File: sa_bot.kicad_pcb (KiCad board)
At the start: 2 copper layers, 120 x 120 mm, 66 parts, among them CON1 MicroSD_Card, P1 USB_OTG, P11 MOTOR_A, P12 MOTOR_B, P13 SONAR_4, P14 SONAR_2, P15 SONAR_3, P17 DBG_CONN, P18 CONN_01X04, P2 BatteryHolder, P3 IR4_JMP, P4 IR2_JMP, P5 IR3_JMP, P6 ExPower, P7 IR_4, P8 IR_2, P9 IR_3, Q1 Q_PMOS_DSG, SW1 SWITCH_INV, SW2 SW_PUSH, SW3 SW_PUSH, U1 74AHC1G125, U2 SAMD21G18, U3 AP2112K-3.3V, U4 NCP1402, U5 DRV8835, Y1 Crystal_Small

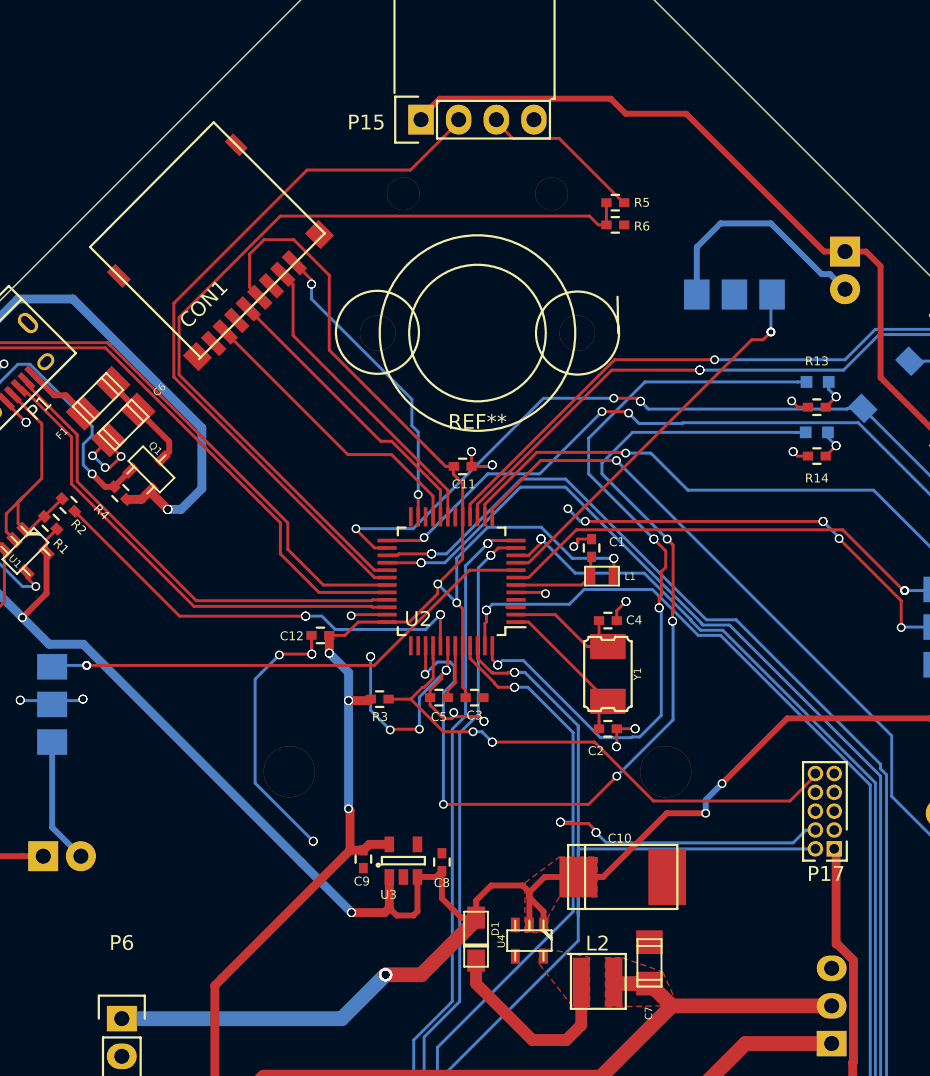
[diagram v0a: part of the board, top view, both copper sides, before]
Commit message: Moved RXTX LEDs
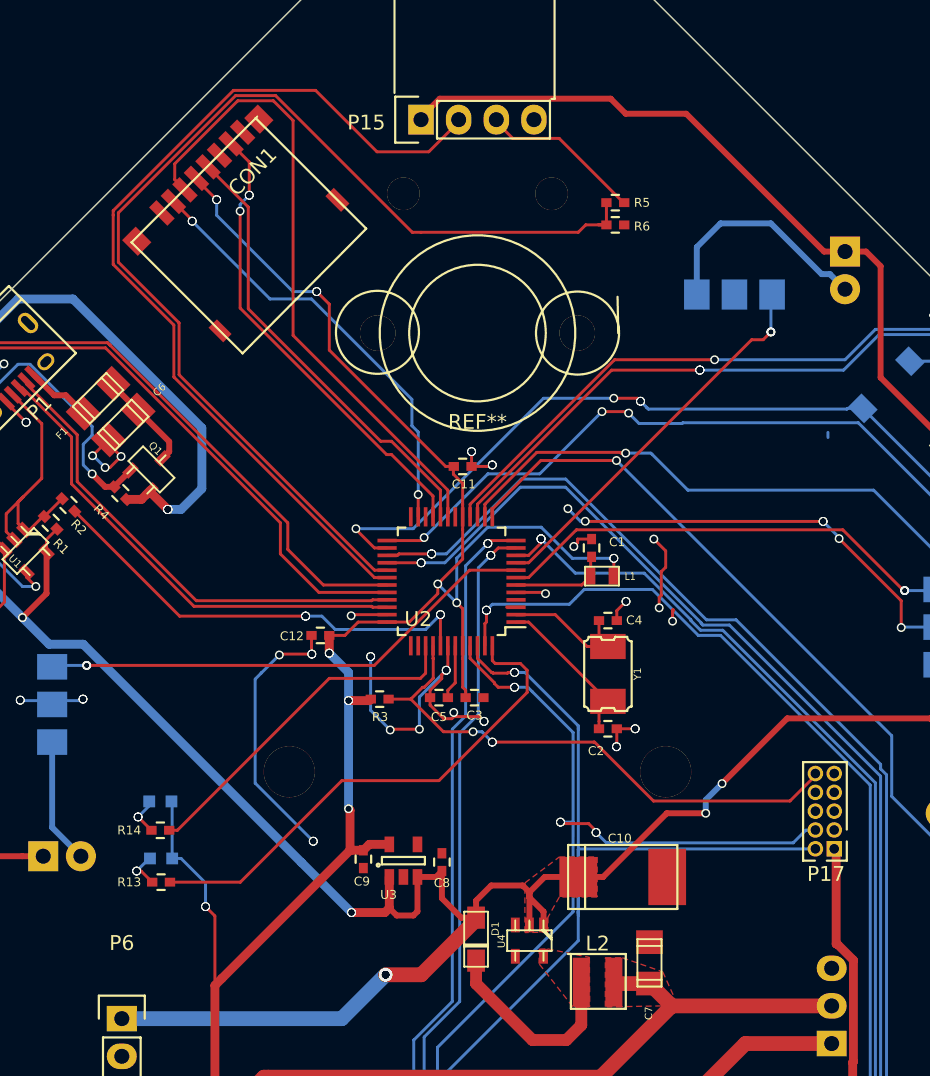
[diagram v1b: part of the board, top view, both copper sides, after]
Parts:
- moved D6 54.7 mm to (118.7, 159.8), turned to 180 degrees
- moved R13 54.6 mm to (118.7, 161.4), turned to 180 degrees
- moved R14 51.0 mm to (118.6, 157.9), turned to 180 degrees
- moved D7 50.8 mm to (118.6, 156.0), turned to 180 degrees
- moved CON1 14.4 mm to (124.2, 110.8), turned to 225 degrees
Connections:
- net /IR1 renamed Net-(U2-Pad3)
- net VCC renamed +5V
- CON1 pad 1: /SD_CS -> Net-(CON1-Pad1)
- CON1 pad 2: /SPI_MOSI -> /SD_CS
- CON1 pad 3: GND -> /SPI_MOSI
- D6 pad 2: /RXLED -> +3V3
- D7 pad 2: /TXLED -> +3V3
- R13 pad 1: GND -> /RXLED
- R14 pad 1: GND -> /TXLED
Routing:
- net /TXLED: track 66.0 -> 23.5 mm, vias 6 -> 0
- net /SPI_MOSI: track 21.0 -> 43.4 mm
- net /RXLED: track 52.8 -> 34.5 mm, vias 6 -> 0
- net /ECHO3: track 56.8 -> 74.4 mm
- net +3V3: track 209.0 -> 224.2 mm, vias 12 -> 18
- net /TRIG3: track 49.4 -> 62.3 mm
- net /SPI_MISO: track 20.0 -> 31.5 mm, vias 0 -> 3
- net /SPI_SCK: track 19.8 -> 30.5 mm
- net /SD_CS: track 20.6 -> 29.8 mm
- net (no net): track 1.16 -> 7.58 mm, vias 2 -> 5
- net GND: track 161.2 -> 158.8 mm, vias 76 -> 73
- net Net-(D7-Pad1): track 2.12 -> 2.63 mm
- added copper zone on F.Cu, net VCC
- removed copper zone on F.Cu, net +5V

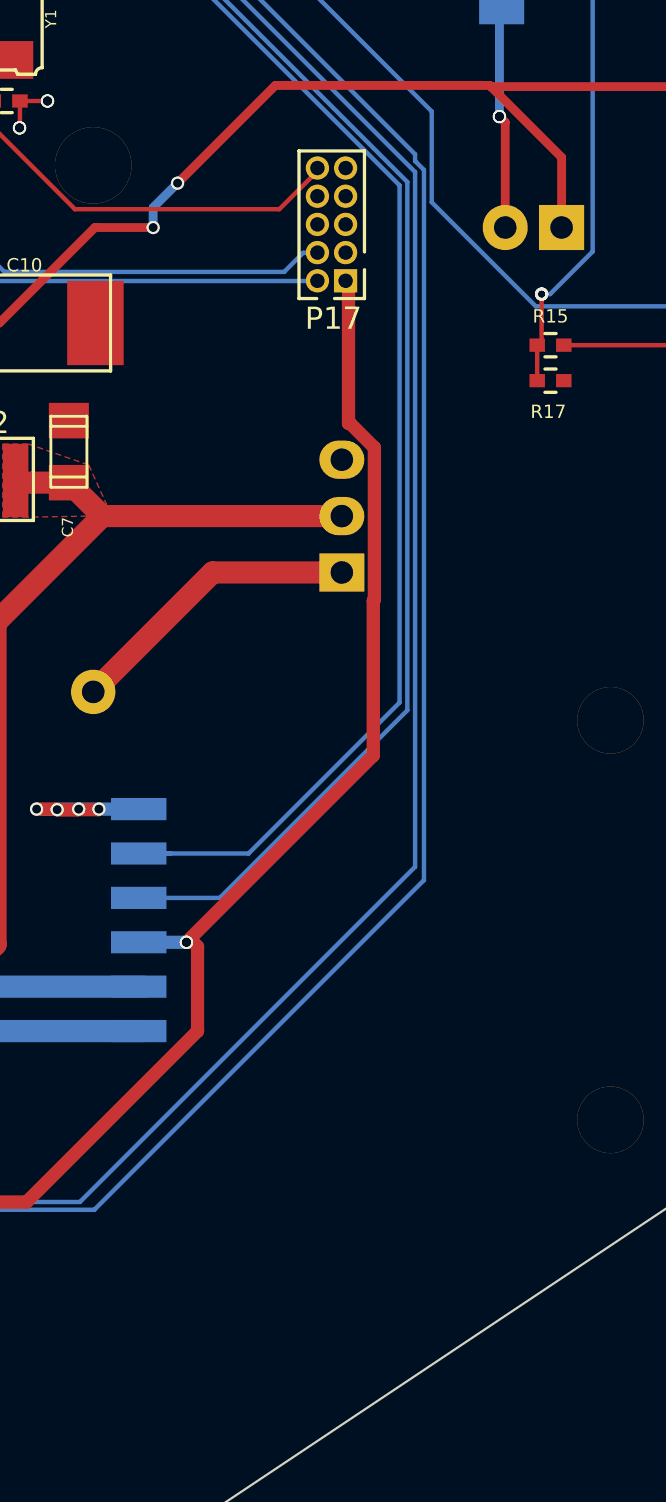
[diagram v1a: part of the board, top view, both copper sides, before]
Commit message: Added Reset Button
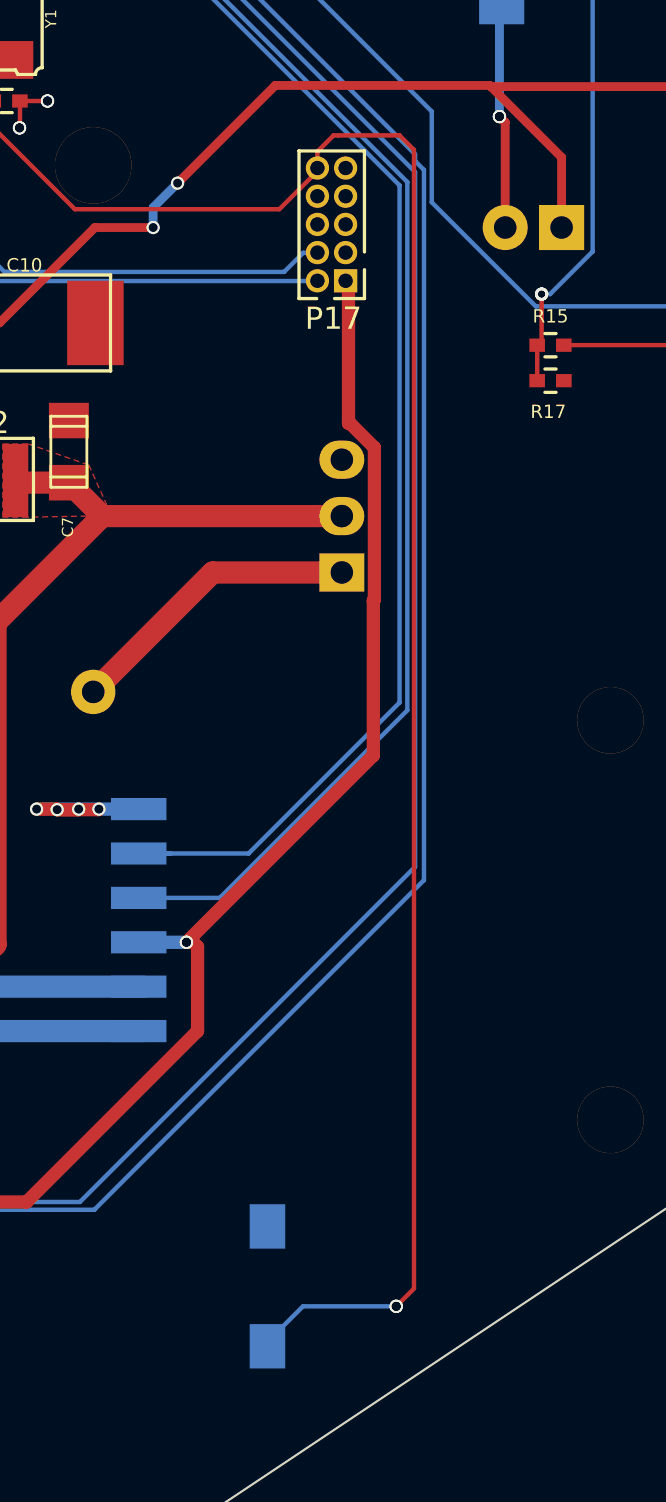
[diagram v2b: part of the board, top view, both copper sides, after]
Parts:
- added RESET: SW_PUSH, Buttons_Switches_SMD:SW_SPST_EVQPE1, B.Cu at (160.6, 204.5)
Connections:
- C10 pad 1: +5V -> VCC
- C8 pad 1: +5V -> VCC
- D1 pad 1: +5V -> VCC
- P13 pad 4: +5V -> VCC
- P14 pad 4: +5V -> VCC
- P15 pad 4: +5V -> VCC
- P18 pad 4: +5V -> VCC
- P3 pad 1: +5V -> VCC
- P4 pad 1: +5V -> VCC
- P5 pad 1: +5V -> VCC
- P6 pad 1: +5V -> VCC
- Q1 pad 2: +5V -> VCC
- R1 pad 1: +5V -> VCC
- R4 pad 1: +5V -> VCC
- U1 pad 5: +5V -> VCC
- U3 pad 1: +5V -> VCC
- U3 pad 3: +5V -> VCC
- U4 pad 1: +5V -> VCC
- U4 pad 2: +5V -> VCC
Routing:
- net VCC: track 0.00 -> 345.1 mm, vias 0 -> 18
- net +5V: track 345.1 -> 0.00 mm, vias 18 -> 0
- net RESET: track 36.8 -> 101.6 mm, vias 3 -> 5

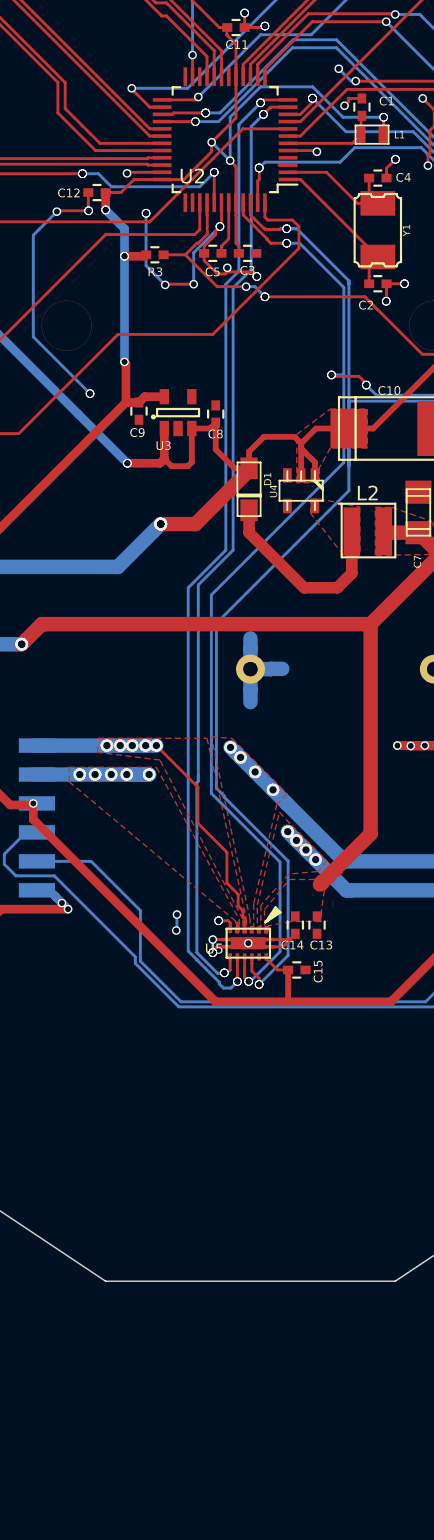
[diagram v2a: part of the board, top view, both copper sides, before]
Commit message: Fixed encoder Interrupt
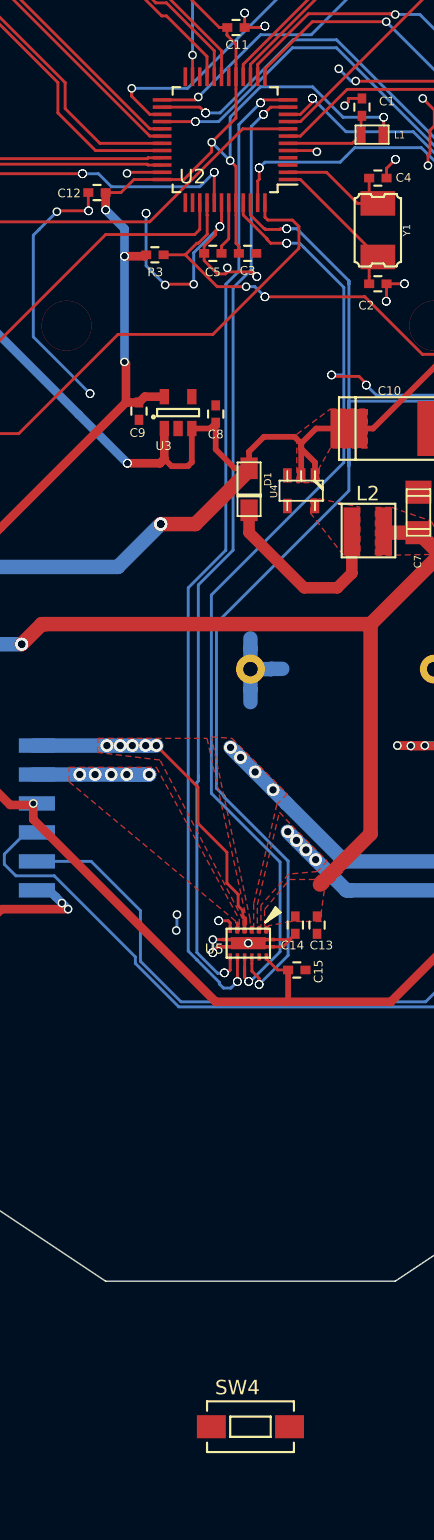
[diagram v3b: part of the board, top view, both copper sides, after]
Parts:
- added SW4: SW_PUSH, Buttons_Switches_SMD:SW_SPST_EVQPE1, F.Cu at (140.0, 230.1)
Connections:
- U2 pad 26: /BUT2 -> /BENC1
- U2 pad 27: /BENC1 -> /BUT2
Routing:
- net /BUT2: track 48.9 -> 49.5 mm
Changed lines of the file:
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@@
 (kicad_pcb (version 4) (host pcbnew "(2015-07-04 BZR 5884, Git c1bbf3e)-product")
   (general
-    (links 168)
-    (no_connects 8)
+    (links 170)
+    (no_connects 10)
     (area 79.949999 99.949999 200.050001 220.050001)
     (thickness 1.6)
     (drawings 17)
-    (tracks 1085)
+    (tracks 1086)
     (zones 0)
-    (modules 67)
+    (modules 68)
     (nets 74)
   )
@@
       (net 55 /BUT1))
     (pad 26 smd rect (at 4.35 2.25 180) (size 1.3 0.25) (layers F.Cu F.Paste F.Mask)
-      (net 56 /BUT2))
-    (pad 27 smd rect (at 4.35 1.75 180) (size 1.3 0.25) (layers F.Cu F.Paste F.Mask)
       (net 28 /BENC1))
+    (pad 27 smd rect (at 4.35 1.75 180) (size 1.3 0.25) (layers F.Cu F.Paste F.Mask)
+      (net 56 /BUT2))
     (pad 28 smd rect (at 4.35 1.25 180) (size 1.3 0.25) (layers F.Cu F.Paste F.Mask)
       (net 29 /BENC2))
@@
       (net 43 RESET))
   )
+  (module Buttons_Switches_SMD:SW_SPST_EVQPE1 (layer F.Cu)
+    (at 140 230.050001)
+    (descr "Light Touch Switch")
+    (attr smd)
+    (fp_text reference SW4 (at -0.9 -2.7) (layer F.SilkS)
+      (effects (font (size 1 1) (thickness 0.15)))
+    )
+    (fp_text value SW_PUSH (at 0 0) (layer F.Fab)
+      (effects (font (size 1 1) (thickness 0.15)))
+    )
+    (fp_line (start -1.4 -0.7) (end 1.4 -0.7) (layer F.SilkS) (width 0.15))
+    (fp_line (start 1.4 -0.7) (end 1.4 0.7) (layer F.SilkS) (width 0.15))
+    (fp_line (start 1.4 0.7) (end -1.4 0.7) (layer F.SilkS) (width 0.15))
+    (fp_line (start -1.4 0.7) (end -1.4 -0.7) (layer F.SilkS) (width 0.15))
+    (fp_line (start -3.95 -2) (end 3.95 -2) (layer F.CrtYd) (width 0.05))
+    (fp_line (start 3.95 -2) (end 3.95 2) (layer F.CrtYd) (width 0.05))
+    (fp_line (start 3.95 2) (end -3.95 2) (layer F.CrtYd) (width 0.05))
+    (fp_line (start -3.95 2) (end -3.95 -2) (layer F.CrtYd) (width 0.05))
+    (fp_line (start 3 -1.75) (end 3 -1.1) (layer F.SilkS) (width 0.15))
+    (fp_line (start 3 1.75) (end 3 1.1) (layer F.SilkS) (width 0.15))
+    (fp_line (start -3 1.1) (end -3 1.75) (layer F.SilkS) (width 0.15))
+    (fp_line (start -3 -1.75) (end -3 -1.1) (layer F.SilkS) (width 0.15))
+    (fp_line (start 3 -1.75) (end -3 -1.75) (layer F.SilkS) (width 0.15))
+    (fp_line (start -3 1.75) (end 3 1.75) (layer F.SilkS) (width 0.15))
+    (pad 2 smd rect (at 2.7 0) (size 2 1.6) (layers F.Cu F.Paste F.Mask)
+      (net 2 GND))
+    (pad 1 smd rect (at -2.7 0) (size 2 1.6) (layers F.Cu F.Paste F.Mask)
+      (net 43 RESET))
+  )
   (gr_text "5V\nGND\nVBATT\n\n" (at 110.8 174.8) (layer B.SilkS)
     (effects (font (size 1.5 1.5) (thickness 0.3)) (justify mirror))
@@
   (segment (start 125 185) (end 128.209651 185) (width 1) (layer B.Cu) (net 27))
   (via (at 128.209651 185) (size 0.89) (drill 0.5) (layers F.Cu B.Cu) (net 27))
-  (segment (start 136.9 139.3) (end 137.9 139.3) (width 0.2) (layer B.Cu) (net 28))
+  (segment (start 133.9 138.9) (end 136.5 138.9) (width 0.2) (layer F.Cu) (net 28))
+  (segment (start 136.5 138.9) (end 136.9 139.3) (width 0.2) (layer F.Cu) (net 28))
   (segment (start 123 191.2) (end 123 190.5) (width 0.2) (layer B.Cu) (net 28))
-  (segment (start 137.9 139.3) (end 142.949989 134.250011) (width 0.2) (layer B.Cu) (net 28))
-  (segment (start 167.2 153.805012) (end 167.6 154.205012) (width 0.2) (layer B.Cu) (net 28))
   (segment (start 132.04999 198.044978) (end 132.04999 197.59999) (width 0.2) (layer B.Cu) (net 28))
-  (segment (start 142.949989 134.250011) (end 145.950011 134.250011) (width 0.2) (layer B.Cu) (net 28))
-  (segment (start 167.6 154.205012) (end 167.6 186.2) (width 0.2) (layer B.Cu) (net 28))
-  (segment (start 145.950011 134.250011) (end 155.44997 143.74997) (width 0.2) (layer B.Cu) (net 28))
-  (segment (start 157.44997 143.74997) (end 167.2 153.5) (width 0.2) (layer B.Cu) (net 28))
-  (segment (start 155.44997 143.74997) (end 157.44997 143.74997) (width 0.2) (layer B.Cu) (net 28))
   (segment (start 135.055022 201.05001) (end 132.04999 198.044978) (width 0.2) (layer B.Cu) (net 28))
   (segment (start 124.5 189) (end 125 189) (width 0.2) (layer B.Cu) (net 28))
-  (segment (start 167.2 153.5) (end 167.2 153.805012) (width 0.2) (layer B.Cu) (net 28))
-  (segment (start 167.6 186.2) (end 152.74999 201.05001) (width 0.2) (layer B.Cu) (net 28))
   (segment (start 152.74999 201.05001) (end 135.055022 201.05001) (width 0.2) (layer B.Cu) (net 28))
   (segment (start 126.45 192) (end 123.8 192) (width 0.2) (layer B.Cu) (net 28))
@@
   (segment (start 123.8 192) (end 123 191.2) (width 0.2) (layer B.Cu) (net 28))
   (segment (start 123 190.5) (end 124.5 189) (width 0.2) (layer B.Cu) (net 28))
+  (segment (start 167.6 154.205012) (end 167.6 186.2) (width 0.2) (layer B.Cu) (net 28))
+  (segment (start 167.6 186.2) (end 152.74999 201.05001) (width 0.2) (layer B.Cu) (net 28))
+  (segment (start 136.9 139.3) (end 137.9 139.3) (width 0.2) (layer B.Cu) (net 28))
+  (segment (start 137.9 139.3) (end 142.949989 134.250011) (width 0.2) (layer B.Cu) (net 28))
+  (segment (start 167.2 153.805012) (end 167.6 154.205012) (width 0.2) (layer B.Cu) (net 28))
+  (segment (start 142.949989 134.250011) (end 145.950011 134.250011) (width 0.2) (layer B.Cu) (net 28))
+  (segment (start 145.950011 134.250011) (end 155.44997 143.74997) (width 0.2) (layer B.Cu) (net 28))
+  (segment (start 157.44997 143.74997) (end 167.2 153.5) (width 0.2) (layer B.Cu) (net 28))
+  (segment (start 155.44997 143.74997) (end 157.44997 143.74997) (width 0.2) (layer B.Cu) (net 28))
+  (segment (start 167.2 153.5) (end 167.2 153.805012) (width 0.2) (layer B.Cu) (net 28))
   (via (at 136.9 139.3) (size 0.6) (drill 0.4) (layers F.Cu B.Cu) (net 28))
-  (segment (start 136.9 139.3) (end 134.7 139.3) (width 0.2) (layer F.Cu) (net 28))
-  (segment (start 134.7 139.3) (end 134.6 139.4) (width 0.2) (layer F.Cu) (net 28))
-  (segment (start 134.6 139.4) (end 133.9 139.4) (width 0.2) (layer F.Cu) (net 28))
   (via (at 136.9 139.3) (size 0.6) (drill 0.4) (layers F.Cu B.Cu) (net 28))
   (via (at 136.9 139.3) (size 0.6) (drill 0.4) (layers F.Cu B.Cu) (net 28))
@@
   (segment (start 136.2 138.4) (end 136.4 138.2) (width 0.2) (layer F.Cu) (net 55))
   (via (at 136.4 138.2) (size 0.6) (drill 0.4) (layers F.Cu B.Cu) (net 55))
+  (segment (start 133.9 139.4) (end 133.05 139.4) (width 0.2) (layer F.Cu) (net 56))
+  (segment (start 133.05 139.4) (end 131.8 138.15) (width 0.2) (layer F.Cu) (net 56))
+  (segment (start 131.8 138.15) (end 131.8 138.024264) (width 0.2) (layer F.Cu) (net 56))
+  (segment (start 131.8 138.024264) (end 131.8 137.6) (width 0.2) (layer F.Cu) (net 56))
+  (segment (start 131.85 137.7) (end 131.85 137.65) (width 0.2) (layer F.Cu) (net 56))
+  (segment (start 131.85 137.65) (end 131.8 137.6) (width 0.2) (layer F.Cu) (net 56))
   (segment (start 151 129) (end 151.408479 129.408479) (width 0.2) (layer B.Cu) (net 56))
   (segment (start 151.408479 129.408479) (end 151.480241 129.480241) (width 0.2) (layer B.Cu) (net 56))
@@
   (segment (start 144.459998 128.8) (end 149.2 128.8) (width 0.2) (layer B.Cu) (net 56))
   (via (at 149.2 128.8) (size 0.6) (drill 0.4) (layers F.Cu B.Cu) (net 56))
-  (segment (start 131.85 137.7) (end 131.85 137.65) (width 0.2) (layer F.Cu) (net 56))
-  (segment (start 131.85 137.65) (end 131.8 137.6) (width 0.2) (layer F.Cu) (net 56))
   (via (at 131.8 137.6) (size 0.6) (drill 0.4) (layers F.Cu B.Cu) (net 56))
-  (segment (start 133.9 138.9) (end 133.05 138.9) (width 0.2) (layer F.Cu) (net 56))
-  (segment (start 133.05 138.9) (end 131.85 137.7) (width 0.2) (layer F.Cu) (net 56))
   (segment (start 167.1 124.5) (end 171.8 124.5) (width 0.2) (layer B.Cu) (net 57))
   (segment (start 171.8 124.5) (end 175.207898 127.907898) (width 0.2) (layer B.Cu) (net 57))
